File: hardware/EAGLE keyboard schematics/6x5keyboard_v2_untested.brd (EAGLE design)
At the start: 117.8 x 116.8 mm, 71 parts

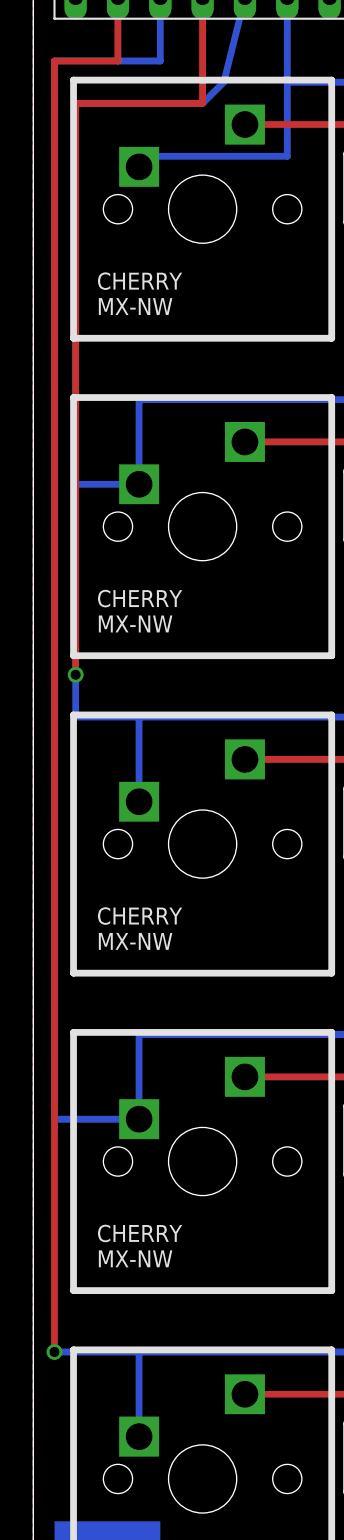
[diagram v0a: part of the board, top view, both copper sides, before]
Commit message: Removed some vias
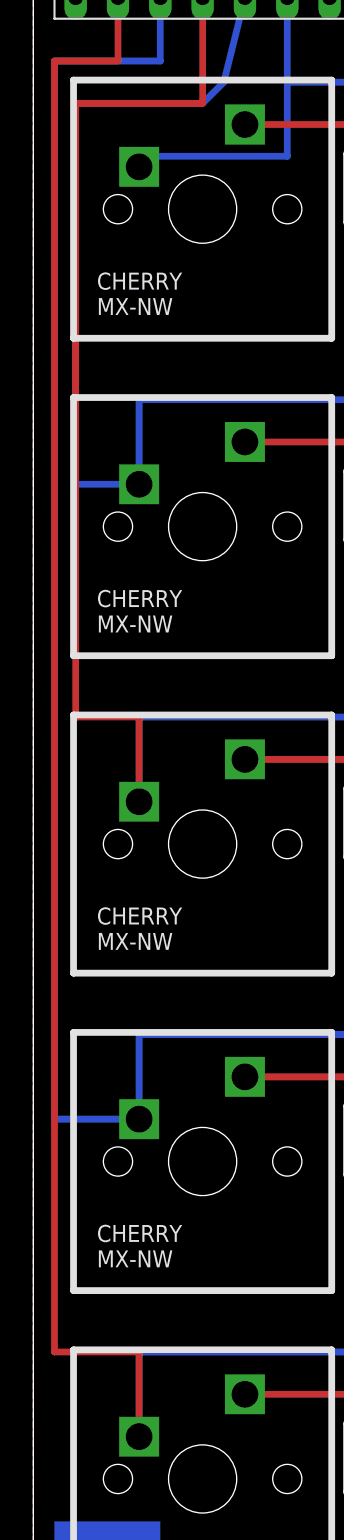
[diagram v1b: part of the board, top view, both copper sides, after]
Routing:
- net N$41: track 215.9 -> 221.0 mm, vias 1 -> 0
- net N$38: track 180.3 -> 185.4 mm, vias 1 -> 0
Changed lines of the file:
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@@
 <?xml version="1.0" encoding="utf-8"?>
 <!DOCTYPE eagle SYSTEM "eagle.dtd">
-<eagle version="6.4">
+<eagle version="6.5.0">
 <drawing>
 <settings>
@@
 <wire x1="11.43" y1="113.03" x2="11.43" y2="106.68" width="0.4064" layer="1"/>
 <wire x1="11.43" y1="106.68" x2="3.81" y2="106.68" width="0.4064" layer="1"/>
-<wire x1="3.81" y1="106.68" x2="3.81" y2="72.39" width="0.4064" layer="1"/>
-<via x="3.81" y="72.39" extent="1-16" drill="0.6" shape="square"/>
-<wire x1="3.81" y1="72.39" x2="3.81" y2="69.85" width="0.4064" layer="16"/>
-<wire x1="3.81" y1="69.85" x2="7.62" y2="69.85" width="0.4064" layer="16"/>
+<wire x1="3.81" y1="106.68" x2="3.81" y2="69.85" width="0.4064" layer="1"/>
+<wire x1="3.81" y1="69.85" x2="7.62" y2="69.85" width="0.4064" layer="1"/>
+<wire x1="7.62" y1="69.85" x2="7.62" y2="64.77" width="0.4064" layer="1"/>
 </signal>
 <signal name="N$39">
@@
 <wire x1="6.35" y1="109.22" x2="2.54" y2="109.22" width="0.4064" layer="1"/>
 <wire x1="2.54" y1="109.22" x2="2.54" y2="31.75" width="0.4064" layer="1"/>
-<via x="2.54" y="31.75" extent="1-16" drill="0.6" shape="square"/>
-<wire x1="2.54" y1="31.75" x2="7.62" y2="31.75" width="0.4064" layer="16"/>
+<wire x1="2.54" y1="31.75" x2="7.62" y2="31.75" width="0.4064" layer="1"/>
+<wire x1="7.62" y1="31.75" x2="7.62" y2="26.67" width="0.4064" layer="1"/>
 </signal>
 <signal name="GND">

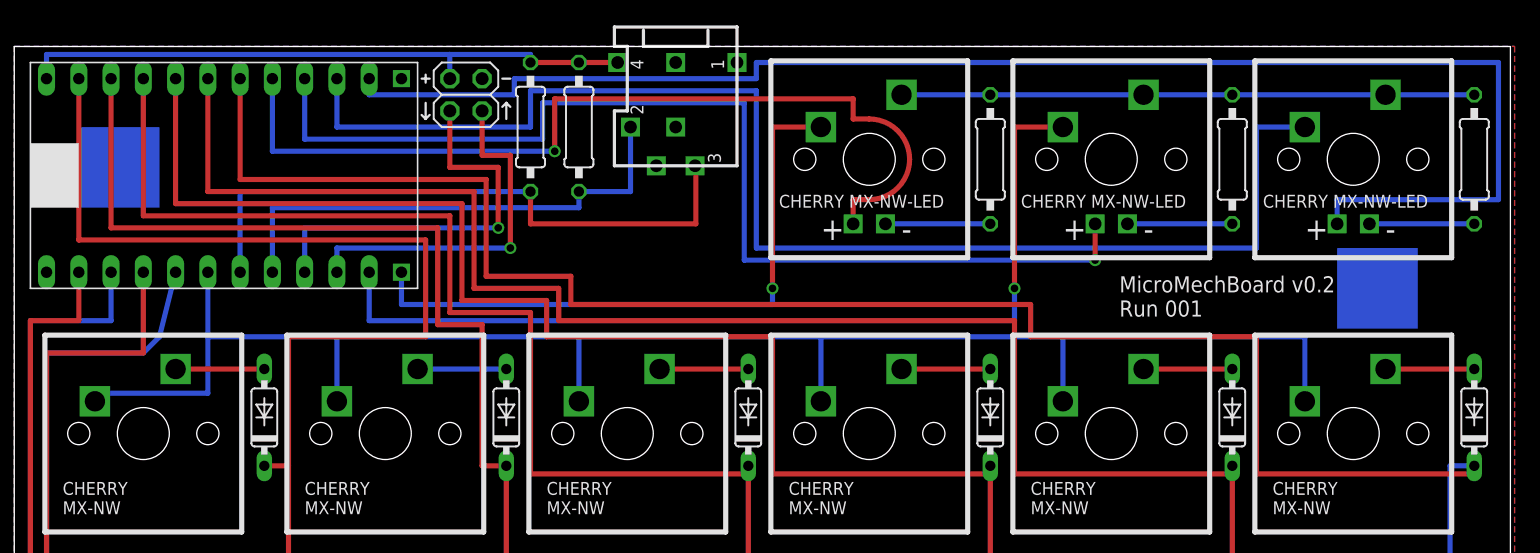
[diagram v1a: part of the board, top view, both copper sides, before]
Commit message: Removed remaining vias :)
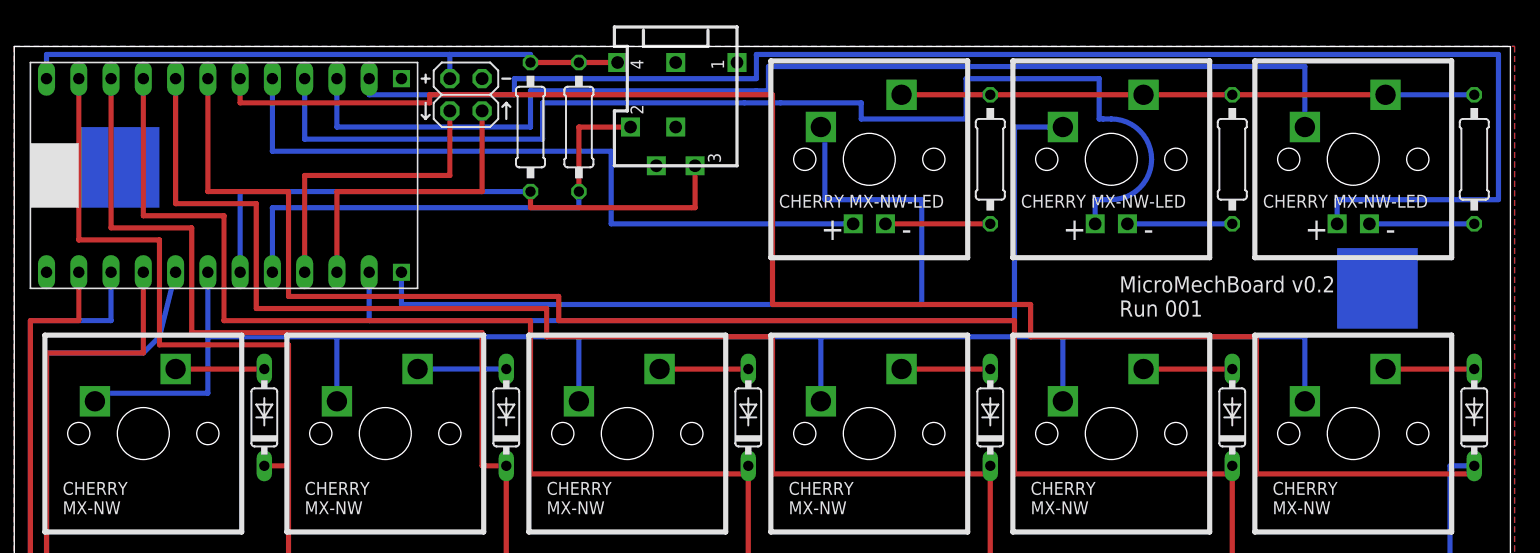
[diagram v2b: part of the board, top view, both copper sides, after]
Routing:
- net N$31: track 154.3 -> 132.7 mm
- net N$50: track 49.5 -> 65.4 mm, vias 1 -> 0
- net N$48: track 104.8 -> 89.5 mm
- net N$47: track 70.6 -> 57.2 mm, vias 1 -> 0
- net N$45: track 31.7 -> 24.1 mm, vias 1 -> 0
- net N$46: track 85.1 -> 90.9 mm, vias 1 -> 0
- net N$55: track 28.6 -> 24.1 mm, vias 1 -> 0
- net N$52: track 49.4 -> 46.7 mm
- net N$54: track 118.1 -> 119.4 mm
- net N$36: track 214.6 -> 215.9 mm
- net N$49: vias 1 -> 0

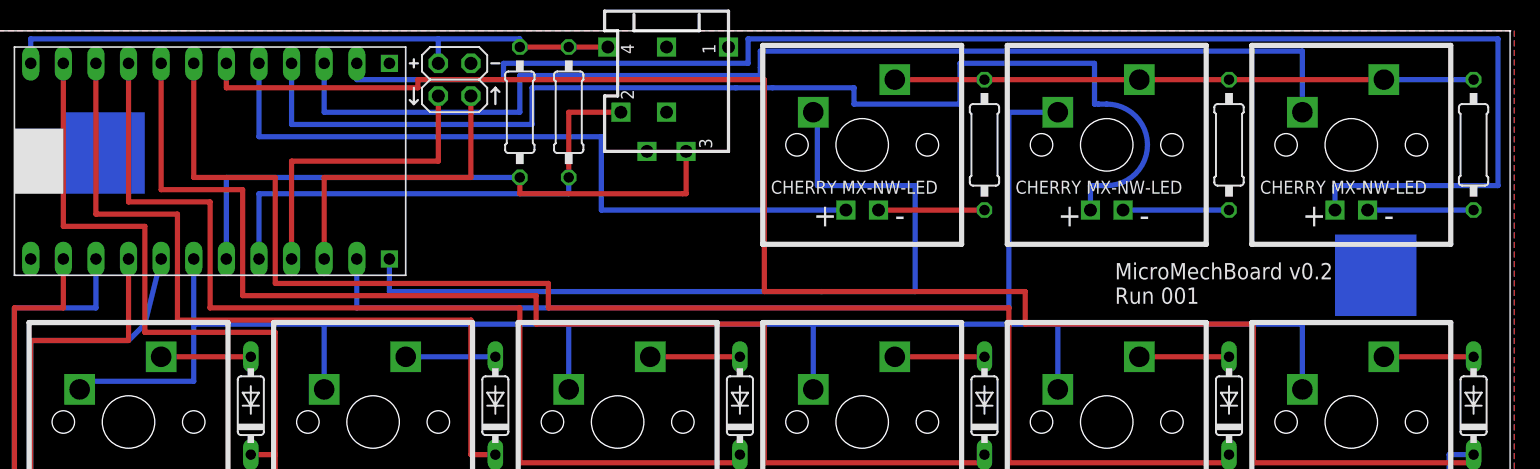
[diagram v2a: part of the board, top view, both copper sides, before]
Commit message: Re-arranged some vias
straightened a few things out
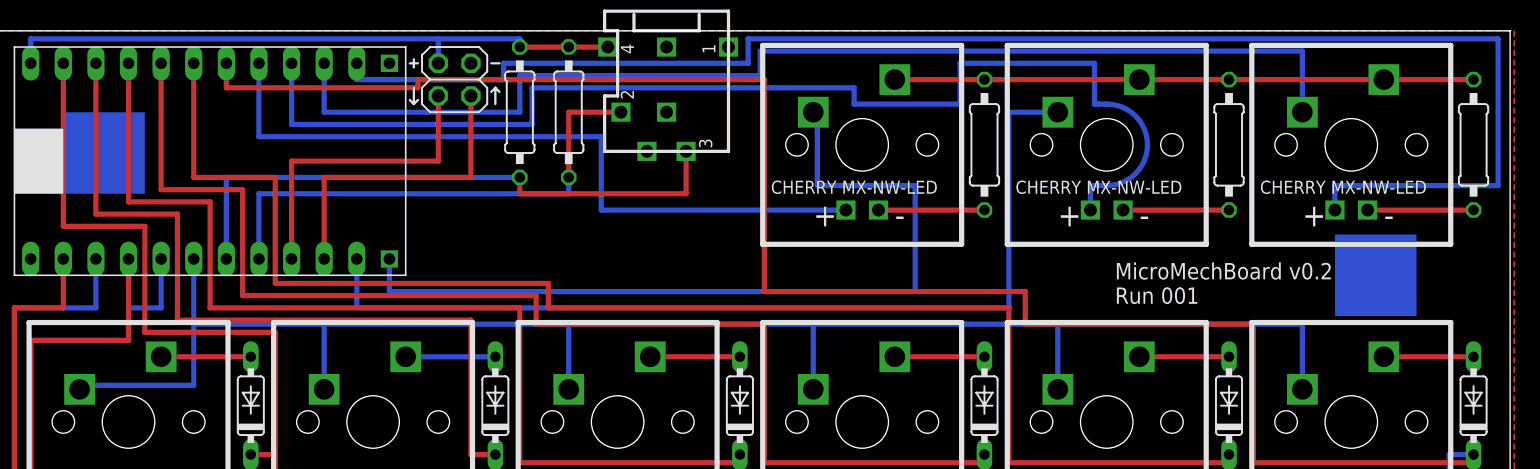
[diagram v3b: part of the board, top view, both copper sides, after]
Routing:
- net N$39: track 167.1 -> 168.9 mm
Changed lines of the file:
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@@
 <contactref element="U$12" pad="SIDE"/>
 <contactref element="U$31" pad="PB3"/>
-<wire x1="13.97" y1="113.03" x2="12.7" y2="107.95" width="0.4064" layer="16"/>
-<wire x1="12.7" y1="107.95" x2="11.43" y2="106.68" width="0.4064" layer="16"/>
 <wire x1="11.43" y1="106.68" x2="3.81" y2="106.68" width="0.4064" layer="16"/>
 <wire x1="3.81" y1="106.68" x2="3.81" y2="83.82" width="0.4064" layer="16"/>
@@
 <wire x1="102.87" y1="83.82" x2="102.87" y2="88.9" width="0.4064" layer="16"/>
 <wire x1="102.87" y1="88.9" x2="83.82" y2="88.9" width="0.4064" layer="16"/>
+<wire x1="13.97" y1="113.03" x2="13.97" y2="109.22" width="0.4064" layer="16"/>
+<wire x1="13.97" y1="109.22" x2="11.43" y2="109.22" width="0.4064" layer="16"/>
+<wire x1="11.43" y1="109.22" x2="11.43" y2="106.68" width="0.4064" layer="16"/>
 </signal>
 <signal name="N$40">
@@
 <contactref element="U$31" pad="PB7"/>
 <wire x1="16.51" y1="113.03" x2="16.51" y2="107.95" width="0.4064" layer="16"/>
-<wire x1="16.51" y1="107.95" x2="16.51" y2="103.505" width="0.4064" layer="16"/>
-<wire x1="16.51" y1="103.505" x2="7.62" y2="103.505" width="0.4064" layer="16"/>
-<wire x1="7.62" y1="103.505" x2="7.62" y2="102.87" width="0.4064" layer="16"/>
+<wire x1="16.51" y1="107.95" x2="16.51" y2="103.1875" width="0.4064" layer="16"/>
+<wire x1="16.51" y1="103.1875" x2="7.62" y2="103.1875" width="0.4064" layer="16"/>
+<wire x1="7.62" y1="103.1875" x2="7.62" y2="102.87" width="0.4064" layer="16"/>
 <wire x1="26.67" y1="102.87" x2="26.67" y2="107.95" width="0.4064" layer="16"/>
 <wire x1="26.67" y1="107.95" x2="16.51" y2="107.95" width="0.4064" layer="16"/>
@@
 <contactref element="R2" pad="1"/>
 <contactref element="R3" pad="1"/>
-<wire x1="109.22" y1="127" x2="116.205" y2="127" width="0.4064" layer="16"/>
 <polygon width="0.4064" layer="16">
 <vertex x="1.27" y="130.81"/>
@@
 <wire x1="90.17" y1="127" x2="97.155" y2="127" width="0.4064" layer="1"/>
 <wire x1="97.155" y1="127" x2="109.22" y2="127" width="0.4064" layer="1"/>
+<wire x1="109.22" y1="127" x2="116.205" y2="127" width="0.4064" layer="1"/>
 </signal>
 <signal name="N$46">
@@
 <contactref element="U$32" pad="LED-"/>
 <contactref element="R1" pad="2"/>
-<wire x1="107.95" y1="116.84" x2="116.205" y2="116.84" width="0.4064" layer="16"/>
+<wire x1="107.95" y1="116.84" x2="116.205" y2="116.84" width="0.4064" layer="1"/>
 </signal>
 <signal name="N$43">
 <contactref element="R2" pad="2"/>
 <contactref element="U$33" pad="LED-"/>
-<wire x1="88.9" y1="116.84" x2="97.155" y2="116.84" width="0.4064" layer="16"/>
+<wire x1="88.9" y1="116.84" x2="97.155" y2="116.84" width="0.4064" layer="1"/>
 </signal>
 <signal name="N$44">

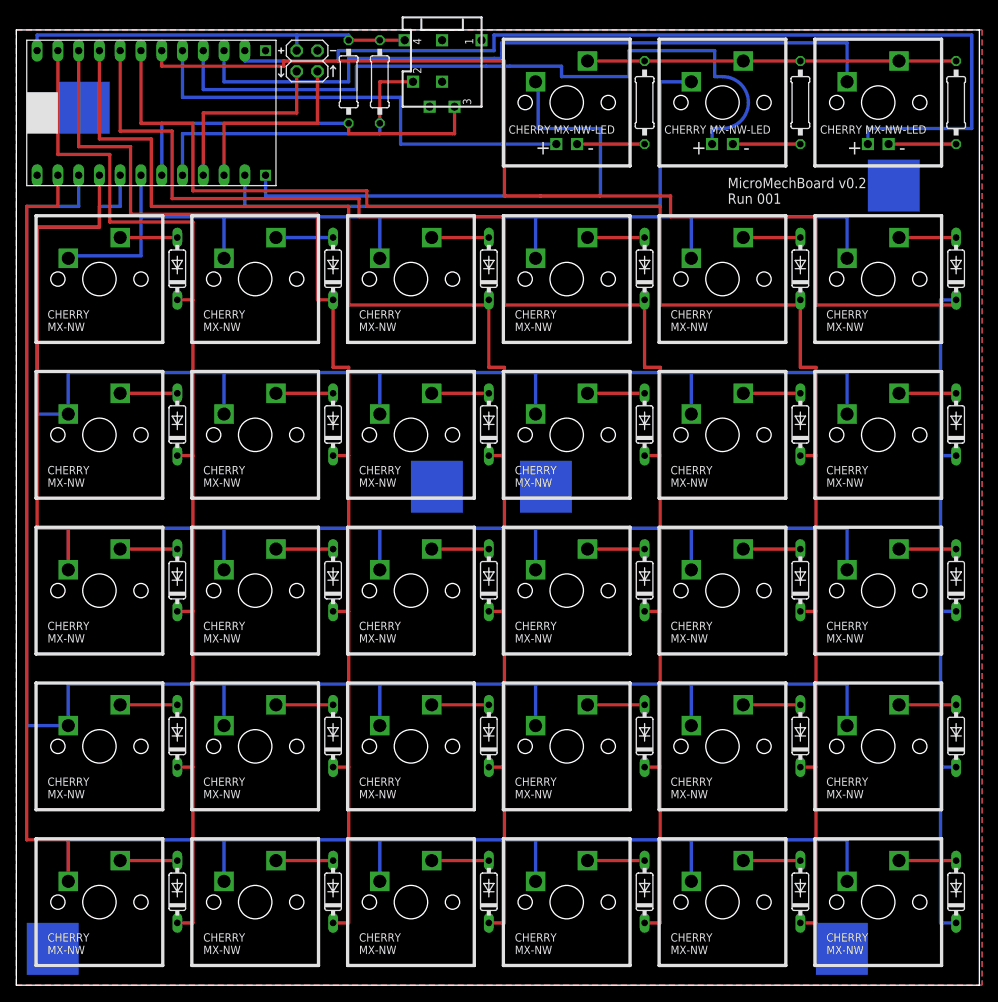
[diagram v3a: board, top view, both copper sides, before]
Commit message: Replaced TRRS connector with dual USB-A connector
Added dual USB-A connector to allow for better daisy-chaining support
(including possible support for hot-swapping). Thanks to CaitSith2 for
assistance.
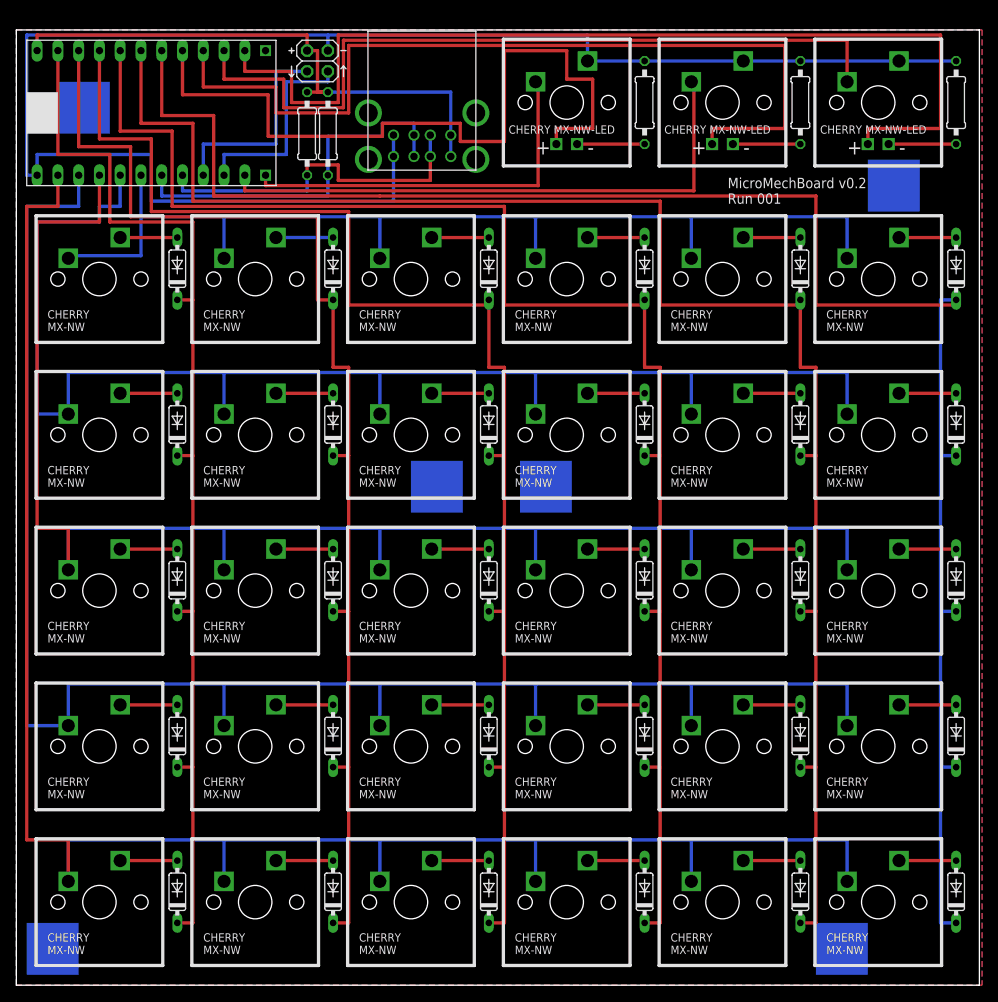
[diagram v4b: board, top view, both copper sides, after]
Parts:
- removed COMM: SJ-43514_HEADPHONES_3.5MM_X4, my_parts:SJ-43514_HEADPHONES-3.5MM_X4
- added U$35: DUAL-USB-A, my_parts:DUAL-USB-A
- moved R4 10.9 mm to (36.8, 118.1)
- moved R5 6.84 mm to (39.4, 118.1)
- moved JP1 1.27 mm to (38.1, 127.0)
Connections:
- removed net N$52: COMM.3, R5.2, U$31.PD0
- removed net N$53: COMM.2, R4.1, U$31.PD1
- new net N$57: R4.1, U$31.PD1, U$35.-DATA_1, U$35.-DATA_2
- new net N$58: R5.2, U$31.PD0, U$35.+DATA_1, U$35.+DATA_2
- net GND: now also U$35.GND_1, U$35.GND_2; no longer COMM.1
- net N$51: now also U$35.VCC_1, U$35.VCC_2; no longer COMM.4
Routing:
- net GND: track 45.1 -> 197.1 mm
- net N$52: track 46.7 -> 0.00 mm
- net N$58: track 0.00 -> 46.3 mm
- net N$57: track 0.00 -> 42.8 mm
- net N$53: track 39.6 -> 0.00 mm
- net N$47: track 57.2 -> 91.8 mm
- net N$51: track 49.4 -> 69.9 mm
- net N$50: track 65.4 -> 47.6 mm
- net N$46: track 90.9 -> 108.0 mm
- net N$48: track 89.5 -> 96.5 mm
- net N$49: track 73.7 -> 70.5 mm
- net N$54: track 119.4 -> 121.9 mm
- net N$36: track 215.9 -> 214.6 mm
- net N$55: track 24.1 -> 25.4 mm
- net N$45: track 24.1 -> 25.4 mm

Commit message: Corrected the ERC warnings.
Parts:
- JP1: value (none) -> UART
- R1, R2, R3: value (none) -> 150
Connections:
- net N$51 renamed VCC
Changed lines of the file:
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@@
 <element name="U$33" library="my_parts" package="CHERRYMX-NN-LED" value="CHERRY-MX1A-E1NW-LED" x="87.63" y="121.92"/>
 <element name="U$34" library="my_parts" package="CHERRYMX-NN-LED" value="CHERRY-MX1A-E1NW-LED" x="68.58" y="121.92"/>
-<element name="R1" library="rcl" package="0207/10" value="" x="116.205" y="121.92" smashed="yes" rot="R270">
-<attribute name="VALUE" x="115.57" y="124.1806" size="1.27" layer="27" ratio="10" rot="R270"/>
+<element name="R1" library="rcl" package="0207/10" value="150" x="116.205" y="121.92" smashed="yes" rot="R270">
+<attribute name="VALUE" x="115.57" y="123.8631" size="1.27" layer="27" font="vector" ratio="18" rot="R270"/>
 </element>
-<element name="R2" library="rcl" package="0207/10" value="" x="97.155" y="121.92" smashed="yes" rot="R270">
-<attribute name="VALUE" x="96.52" y="124.1806" size="1.27" layer="27" ratio="10" rot="R270"/>
+<element name="R2" library="rcl" package="0207/10" value="150" x="97.155" y="121.92" smashed="yes" rot="R270">
+<attribute name="VALUE" x="96.52" y="123.8631" size="1.27" layer="27" font="vector" ratio="18" rot="R270"/>
 </element>
-<element name="R3" library="rcl" package="0207/10" value="" x="78.105" y="121.92" smashed="yes" rot="R270">
-<attribute name="VALUE" x="77.47" y="124.1806" size="1.27" layer="27" ratio="10" rot="R270"/>
+<element name="R3" library="rcl" package="0207/10" value="150" x="78.105" y="121.92" smashed="yes" rot="R270">
+<attribute name="VALUE" x="77.47" y="123.8631" size="1.27" layer="27" font="vector" ratio="18" rot="R270"/>
 </element>
-<element name="R4" library="resistor" package="0207/10" value="3.3K" x="36.83" y="118.11" smashed="yes" rot="R90"/>
-<element name="R5" library="resistor" package="0207/10" value="3.3K" x="39.37" y="118.11" smashed="yes" rot="R270"/>
-<element name="JP1" library="pinhead" package="2X02" value="" x="38.1" y="127" smashed="yes" rot="R270">
-<attribute name="VALUE" x="33.655" y="129.54" size="1.27" layer="27" rot="R270"/>
+<element name="R4" library="resistor" package="0207/10" value="3.3K" x="36.83" y="118.11" smashed="yes" rot="R90">
+<attribute name="VALUE" x="36.195" y="120.3706" size="1.27" layer="27" font="vector" ratio="18" rot="R270"/>
 </element>
+<element name="R5" library="resistor" package="0207/10" value="3.3K" x="39.37" y="118.11" smashed="yes" rot="R270">
+<attribute name="VALUE" x="38.735" y="120.3706" size="1.27" layer="27" font="vector" ratio="18" rot="R270"/>
+</element>
+<element name="JP1" library="pinhead" package="2X02" value="UART" x="38.1" y="127" smashed="yes" rot="R270"/>
 <element name="U$35" library="my_parts" package="DUAL-USB-A" value="DUAL-USB-A" x="57.4675" y="120.65" rot="R180"/>
 </elements>
@@
 <wire x1="49.8975" y1="119.38" x2="49.8975" y2="117.94" width="0.4064" layer="16"/>
 </signal>
-<signal name="N$51">
+<signal name="VCC">
 <contactref element="U$35" pad="VCC_2"/>
 <contactref element="U$35" pad="VCC_1"/>
